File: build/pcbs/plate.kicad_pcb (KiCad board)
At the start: 2 copper layers, 125.2 x 118.7 mm, 42 parts

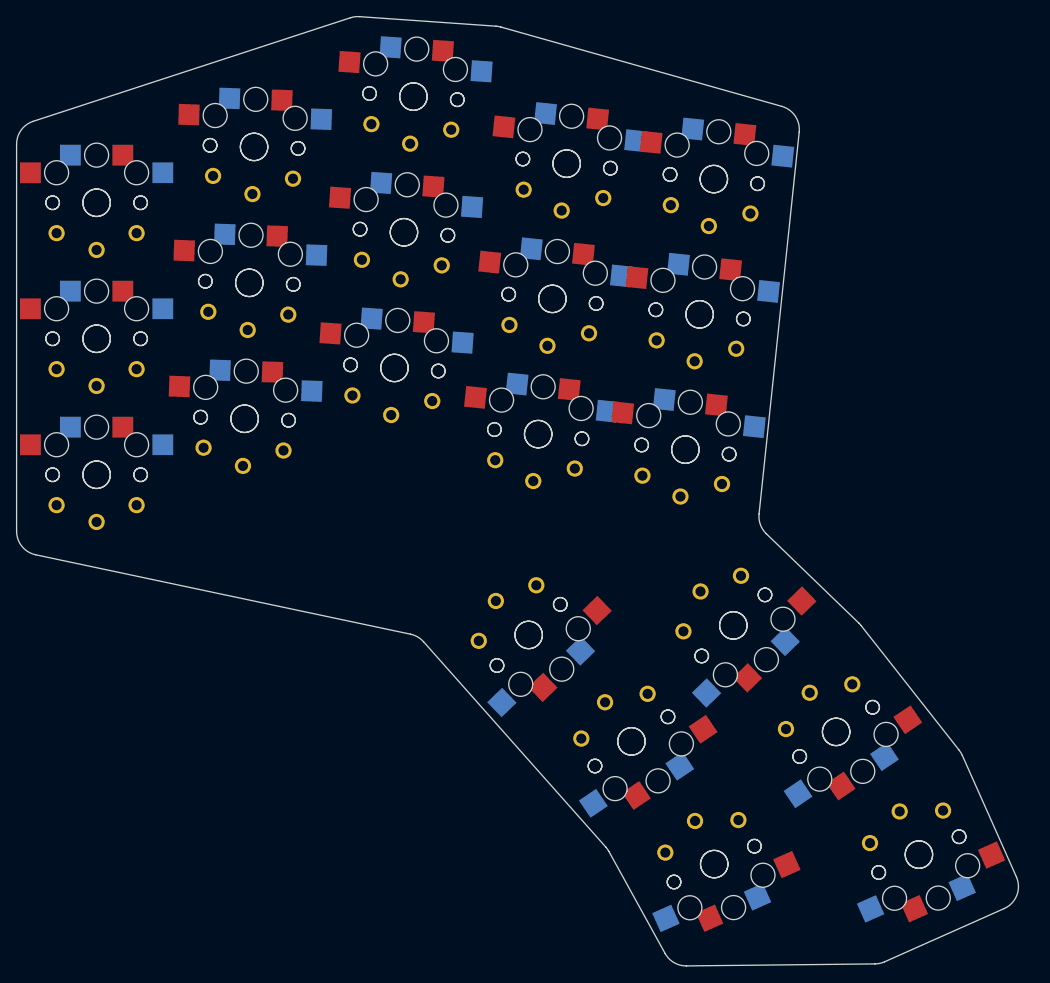
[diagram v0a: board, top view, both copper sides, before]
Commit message: Remove one thumb key, update outelines
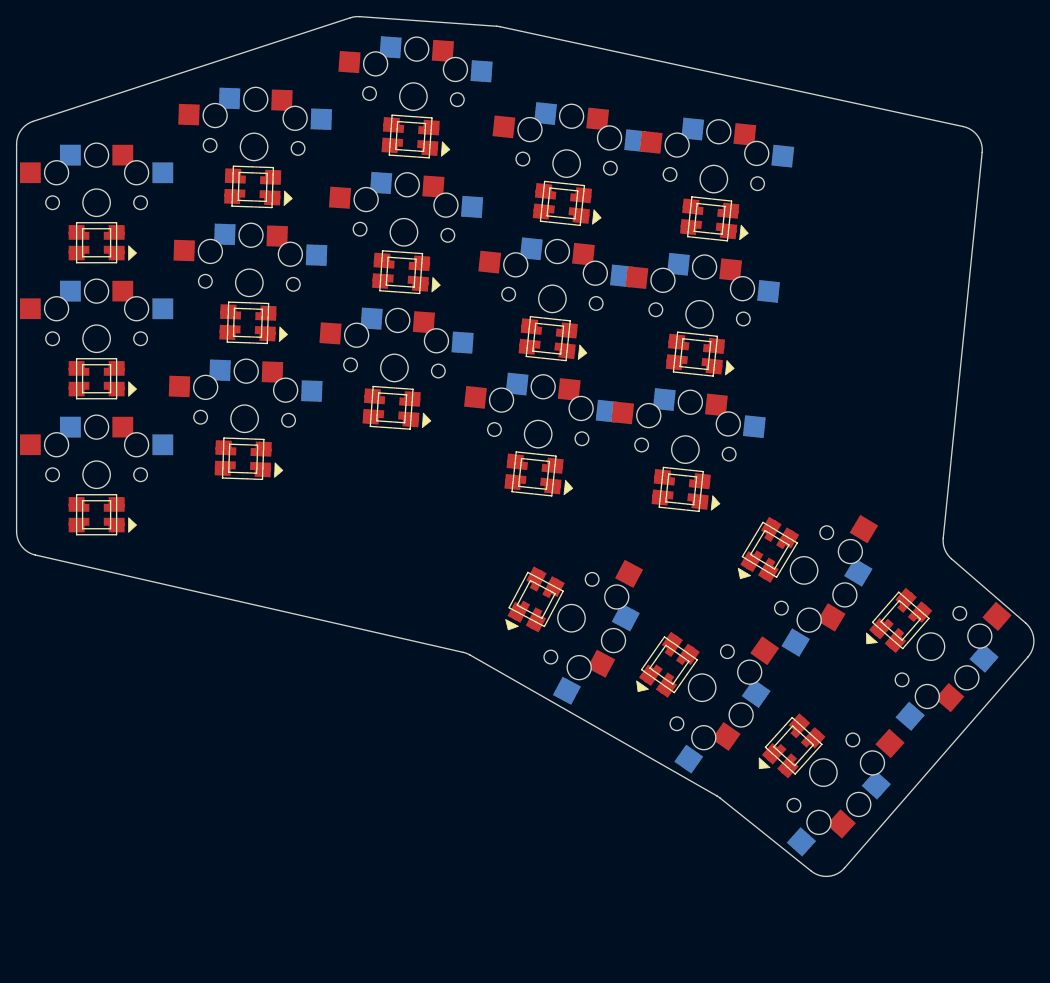
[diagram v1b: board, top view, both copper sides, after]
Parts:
- removed S21, S22, S23, S24, S25, S26, S27, S28, S29, S30, S31, S32, S33, S34, S35, S36, S37, S38, S39, S40, S41, S42: , PG1350
- added LED1: , WS2812B, F.Cu at (0.00, -2.00)
- added LED10: , WS2812B, F.Cu at (54.7, -7.10)
- added LED11: , WS2812B, F.Cu at (56.5, -24.0)
- added LED12: , WS2812B, F.Cu at (58.2, -40.9)
- added LED13: , WS2812B, F.Cu at (73.1, -5.17)
- added LED14: , WS2812B, F.Cu at (74.9, -22.1)
- added LED15: , WS2812B, F.Cu at (76.6, -39.0)
- added LED16: , WS2812B, F.Cu at (84.1, 2.38)
- added LED17: , WS2812B, F.Cu at (100.5, 11.2)
- added LED18: , WS2812B, F.Cu at (54.9, 8.59)
- added LED19: , WS2812B, F.Cu at (71.6, 16.8)
- added LED2: , WS2812B, F.Cu at (0.00, -19.0)
- added LED20: , WS2812B, F.Cu at (87.1, 26.9)
- added LED3: , WS2812B, F.Cu at (0.00, -36.0)
- added LED4: , WS2812B, F.Cu at (18.3, -9.00)
- added LED5: , WS2812B, F.Cu at (18.9, -26.0)
- added LED6: , WS2812B, F.Cu at (19.5, -43.0)
- added LED7: , WS2812B, F.Cu at (36.9, -15.4)
- added LED8: , WS2812B, F.Cu at (38.1, -32.3)
- added LED9: , WS2812B, F.Cu at (39.3, -49.3)
- moved S18 52.5 mm to (59.4, 10.9), turned to -118 degrees
- moved S20 24.3 mm to (90.9, 30.2), turned to -132 degrees
- moved S19 22.7 mm to (75.7, 19.6), turned to -125 degrees
- moved S17 15.9 mm to (104.3, 14.5), turned to -131 degrees
- moved S16 11.2 mm to (88.4, 4.96), turned to -121 degrees
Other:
- board size 125.2 x 118.7 mm -> 127.2 x 107.5 mm

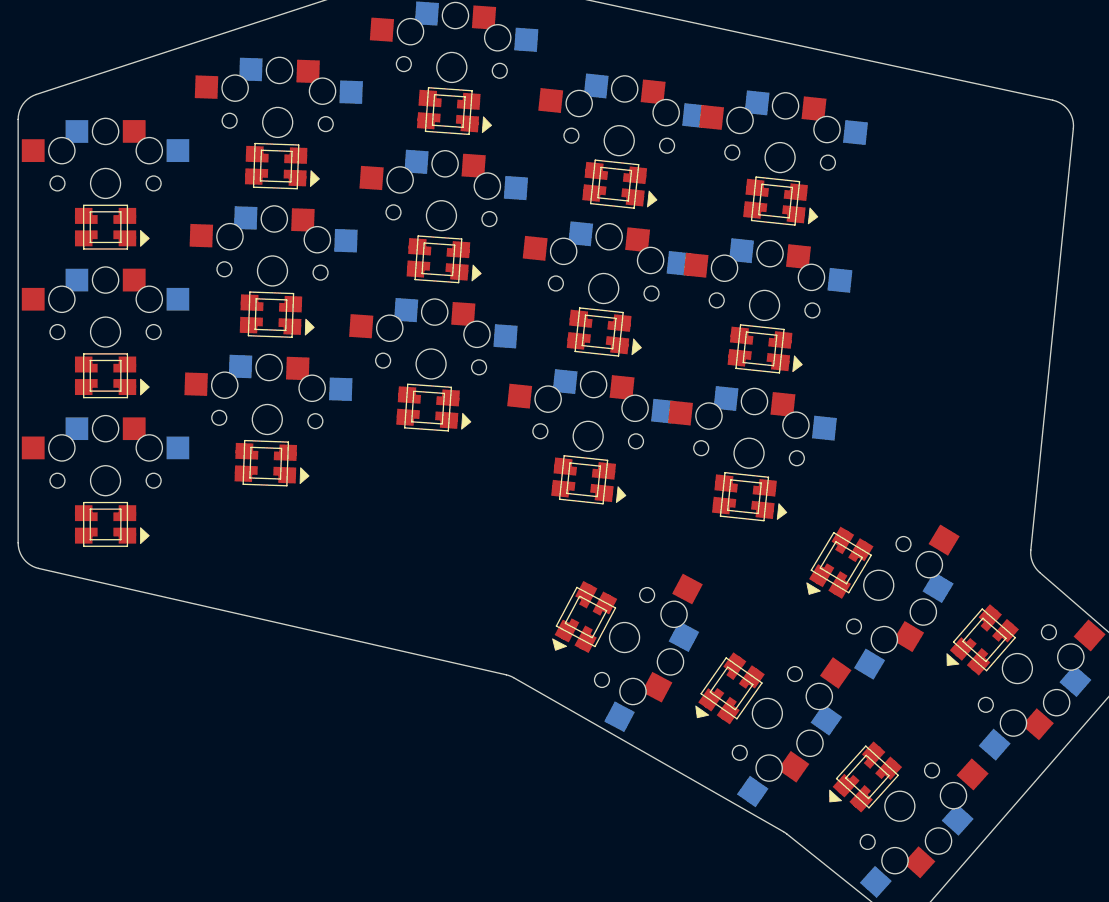
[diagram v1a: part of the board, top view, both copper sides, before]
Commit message: Remove wip rgb
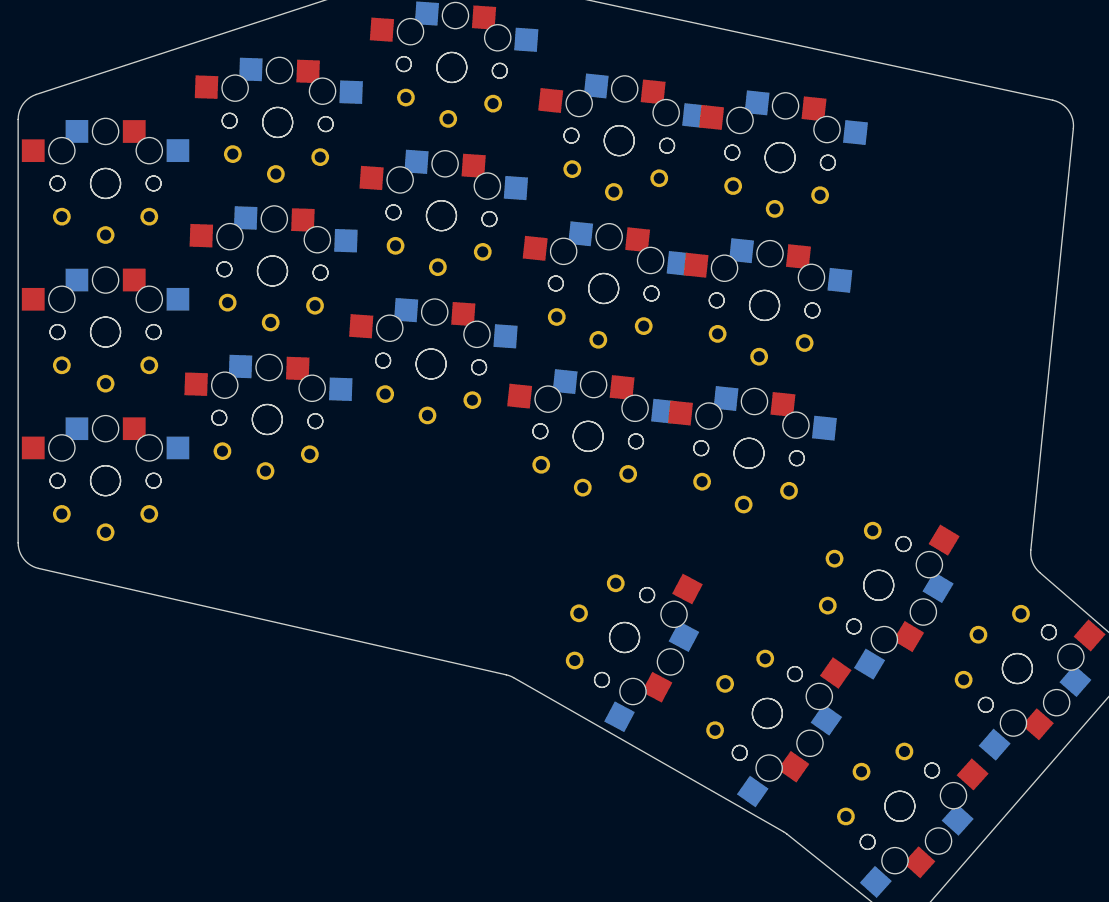
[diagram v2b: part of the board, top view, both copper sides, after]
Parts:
- removed LED1, LED10, LED11, LED12, LED13, LED14, LED15, LED16, LED17, LED18, LED19, LED2, LED20, LED3, LED4, LED5, LED6, LED7, LED8, LED9: , WS2812B
- added S21: , PG1350, F.Cu at (0.00, -7.00)
- added S22: , PG1350, F.Cu at (0.00, -24.0)
- added S23: , PG1350, F.Cu at (0.00, -41.0)
- added S24: , PG1350, F.Cu at (18.5, -14.0)
- added S25: , PG1350, F.Cu at (19.1, -31.0)
- added S26: , PG1350, F.Cu at (19.7, -48.0)
- added S27: , PG1350, F.Cu at (37.2, -20.4)
- added S28: , PG1350, F.Cu at (38.4, -37.3)
- added S29: , PG1350, F.Cu at (39.6, -54.3)
- added S30: , PG1350, F.Cu at (55.2, -12.1)
- added S31: , PG1350, F.Cu at (57.0, -29.0)
- added S32: , PG1350, F.Cu at (58.8, -45.9)
- added S33: , PG1350, F.Cu at (73.6, -10.1)
- added S34: , PG1350, F.Cu at (75.4, -27.0)
- added S35: , PG1350, F.Cu at (77.2, -44.0)
- added S36: , PG1350, F.Cu at (88.4, 4.96)
- added S37: , PG1350, F.Cu at (104.3, 14.5)
- added S38: , PG1350, F.Cu at (59.4, 10.9)
- added S39: , PG1350, F.Cu at (75.7, 19.6)
- added S40: , PG1350, F.Cu at (90.9, 30.2)

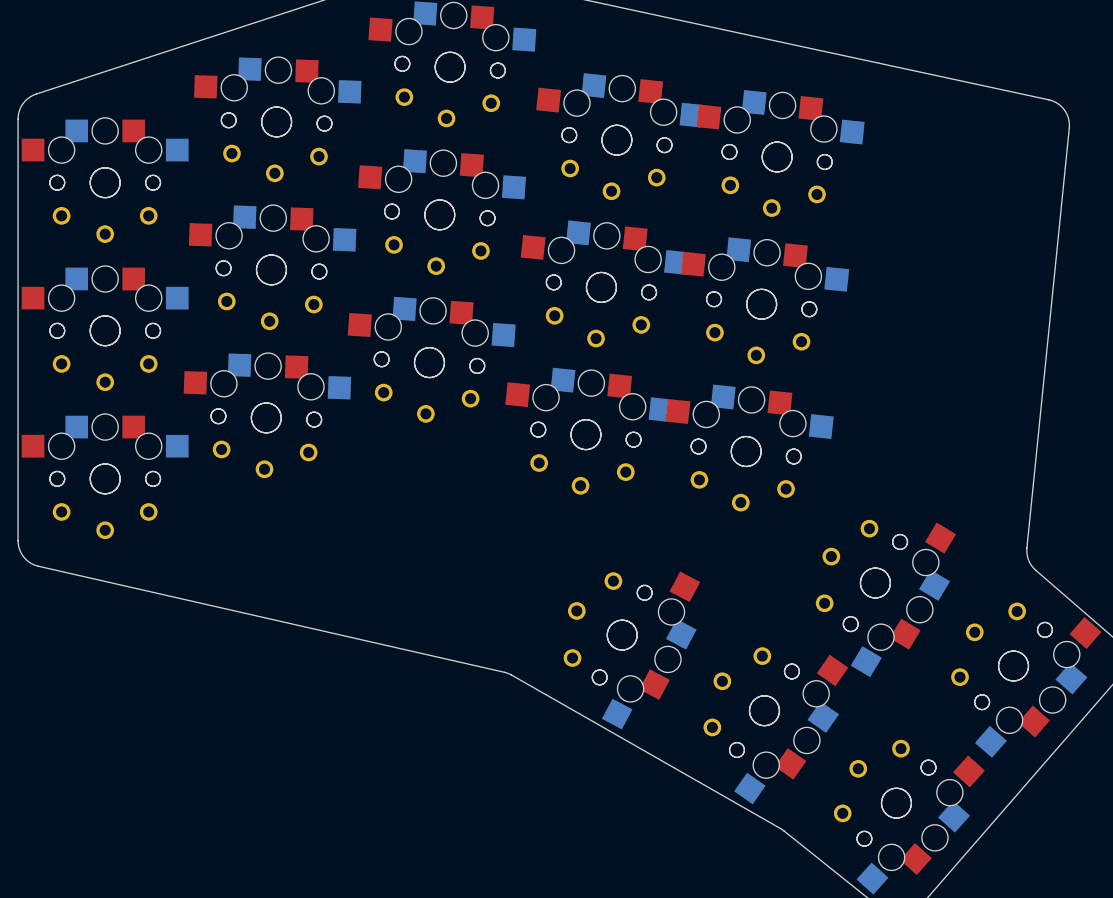
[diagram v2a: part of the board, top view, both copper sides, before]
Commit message: Add EliteC controller
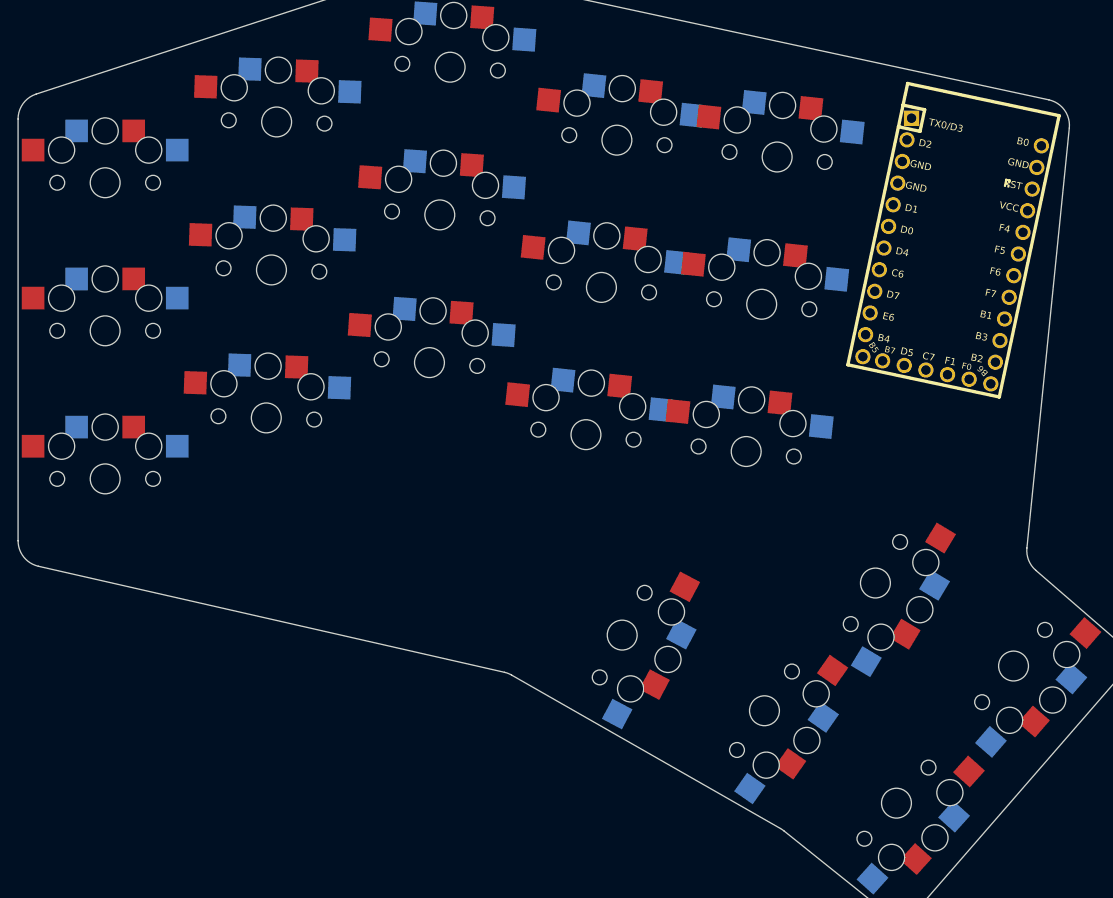
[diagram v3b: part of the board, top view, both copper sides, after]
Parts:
- removed S21, S22, S23, S24, S25, S26, S27, S28, S29, S30, S31, S32, S33, S34, S35, S36, S37, S38, S39, S40: , PG1350
- added MCU1: Elite-C, Elite-C, F.Cu at (97.1, -33.2)
